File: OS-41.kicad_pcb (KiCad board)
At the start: 4 copper layers, 45.2 x 55.8 mm, 79 parts, among them J1 Conn_01x02_Pin, J2 Conn_01x02_Pin, J3 Conn_01x02_Pin, J4 Conn_Coaxial, J5 Conn_01x02_Pin, J6 USB_B_Micro, J7 Conn_01x09_Pin, SW1 TS-1187A-B-A-B, SW2 TS-1187A-B-A-B, U1 GPS1003, U10 W25Q128JVS, U2 SI4432-B1-FMR, U3 MCP1640x-xCHY, U4 ATGM336H-5N31, U5 DS18B20, U6 BMP390L, U7 RP2040, U8 ABM8-272-T3_C20625731, U9 AMS1117-3.3, X1 SMD-3225_4P 30.000MHZ 10PF

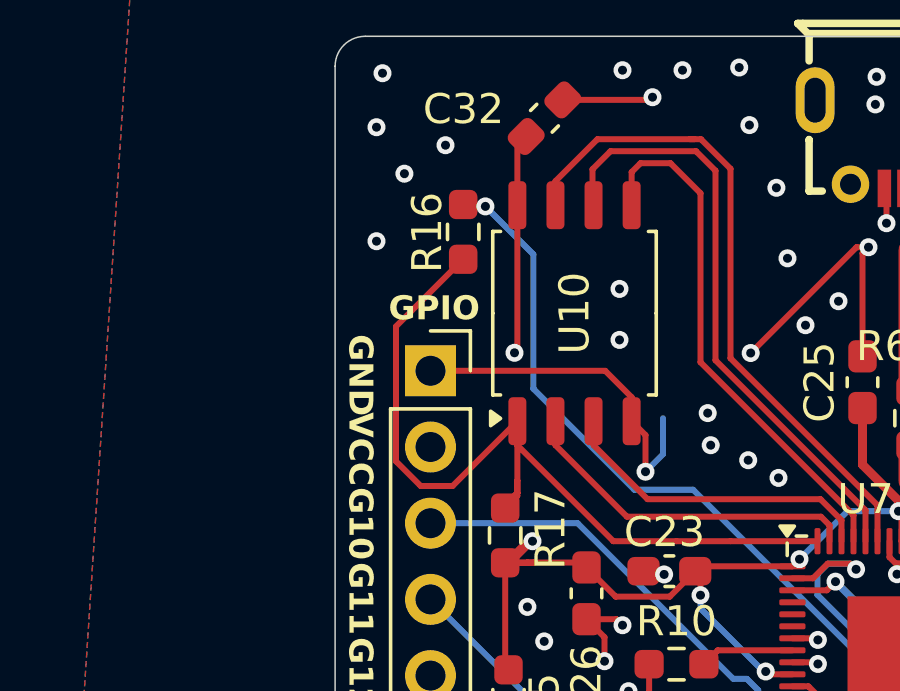
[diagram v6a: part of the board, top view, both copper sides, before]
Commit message: Fixed up some routing
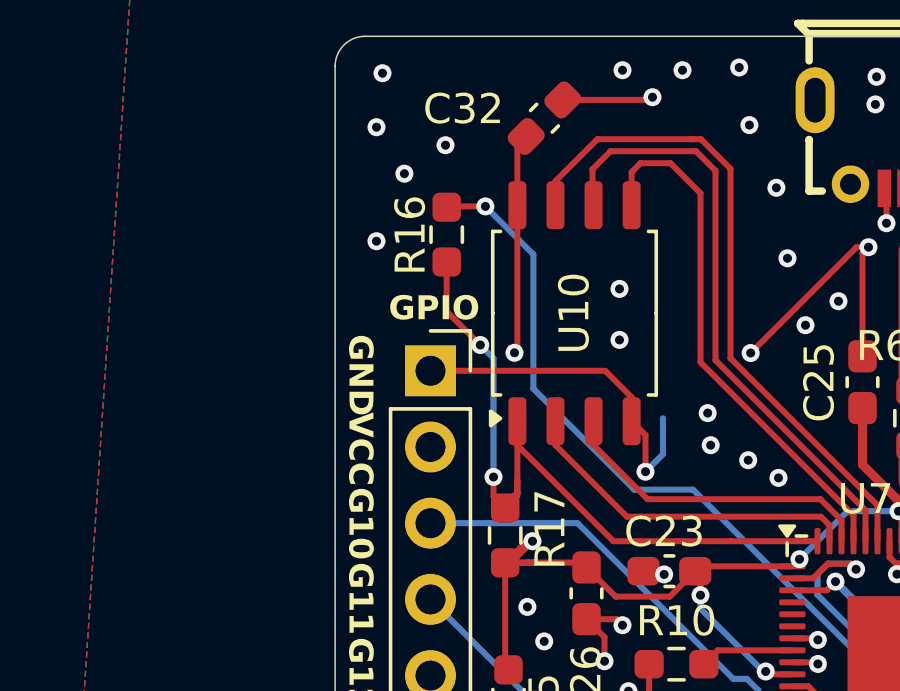
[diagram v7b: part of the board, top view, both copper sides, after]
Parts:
- moved R16 0.56 mm to (96.5, 93.0)
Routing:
- net QSPI_SS: track 29.9 -> 26.0 mm, vias 0 -> 2
- net USB_BOOT: track 44.3 -> 44.9 mm
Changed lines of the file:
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@@
 	(footprint "Resistor_SMD:R_0603_1608Metric_Pad0.98x0.95mm_HandSolder"
 		(layer "F.Cu")
-		(at 97.09 92.89 -90)
+		(at 96.54 92.98 -90)
 		(descr "Resistor SMD 0603 (1608 Metric), square (rectangular) end terminal, IPC_7351 nominal with elongated pad for handsoldering. (Body size source: IPC-SM-782 page 72, https://www.pcb-3d.com/wordpress/wp-content/uploads/ipc-sm-782a_amendment_1_and_2.pdf), generated with kicad-footprint-generator")
 		(tags "resistor handsolder")
@@
 	)
 	(segment
-		(start 97.1525 92.04)
-		(end 97.09 91.9775)
+		(start 97.83 92.04)
+		(end 96.5675 92.04)
 		(width 0.2)
 		(layer "F.Cu")
@@
 	)
 	(segment
-		(start 97.83 92.04)
-		(end 97.1525 92.04)
+		(start 121.55 109.8075)
+		(end 121.55 109.27)
 		(width 0.2)
 		(layer "F.Cu")
@@
 	)
 	(segment
-		(start 121.55 109.8075)
-		(end 121.55 109.27)
+		(start 96.5675 92.04)
+		(end 96.54 92.0675)
 		(width 0.2)
 		(layer "F.Cu")
@@
 	)
 	(segment
-		(start 96.735 101.36)
-		(end 98.895 99.2)
+		(start 98.895 99.2)
+		(end 98.895 99.999999)
 		(width 0.2)
 		(layer "F.Cu")
@@
 	)
 	(segment
-		(start 98.895 99.2)
-		(end 98.895 99.999999)
+		(start 96.54 93.8925)
+		(end 96.54 95.54)
 		(width 0.2)
 		(layer "F.Cu")
@@
 	)
 	(segment
-		(start 94.85 96.0425)
-		(end 94.85 100.536347)
-		(width 0.2)
-		(layer "F.Cu")
-		(net 33)
-	)
-	(segment
 		(start 98.895 101.69)
 		(end 98.49 102.095)
@@
 	)
 	(segment
-		(start 97.09 93.8025)
-		(end 94.85 96.0425)
+		(start 98.1 101.705)
+		(end 98.49 102.095)
 		(width 0.2)
 		(layer "F.Cu")
@@
 	)
 	(segment
-		(start 94.85 100.536347)
-		(end 95.673653 101.36)
+		(start 98.1 101.06)
+		(end 98.1 101.705)
 		(width 0.2)
 		(layer "F.Cu")
@@
 	)
 	(segment
-		(start 98.895 101.18)
-		(end 98.895 101.69)
+		(start 96.54 95.54)
+		(end 97.66 96.66)
 		(width 0.2)
 		(layer "F.Cu")
@@
 	)
 	(segment
-		(start 95.673653 101.36)
-		(end 96.735 101.36)
+		(start 98.895 101.18)
+		(end 98.895 101.69)
 		(width 0.2)
 		(layer "F.Cu")
@@
 		(net 33)
 	)
+	(via
+		(at 98.1 101.06)
+		(size 0.6)
+		(drill 0.3)
+		(layers "F.Cu" "B.Cu")
+		(net 33)
+	)
+	(via
+		(at 97.66 96.66)
+		(size 0.6)
+		(drill 0.3)
+		(layers "F.Cu" "B.Cu")
+		(net 33)
+	)
+	(segment
+		(start 97.66 96.66)
+		(end 98.1 97.1)
+		(width 0.2)
+		(layer "B.Cu")
+		(net 33)
+	)
+	(segment
+		(start 98.1 97.1)
+		(end 98.1 101.06)
+		(width 0.2)
+		(layer "B.Cu")
+		(net 33)
+	)

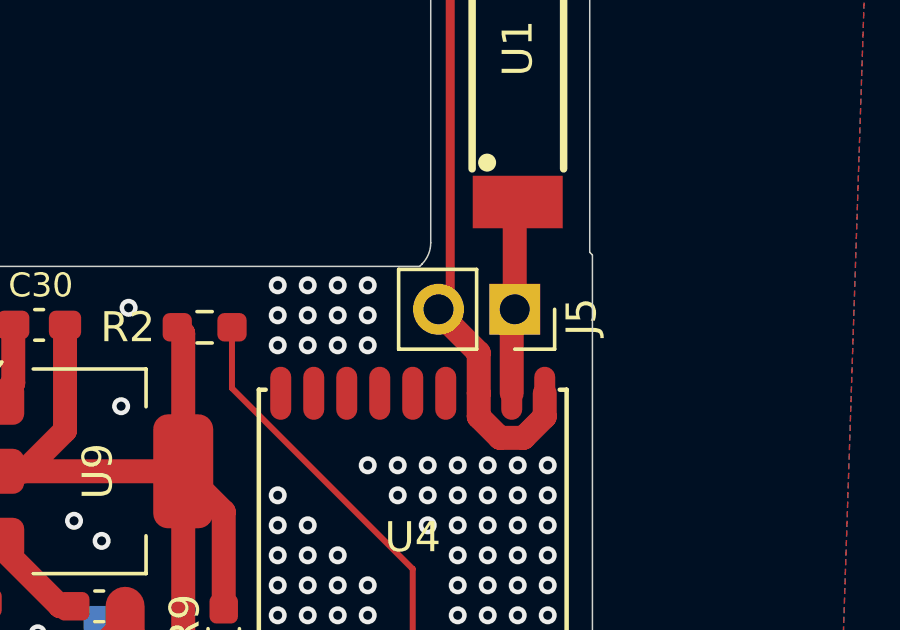
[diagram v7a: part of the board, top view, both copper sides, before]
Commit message: Add GPS ANT text
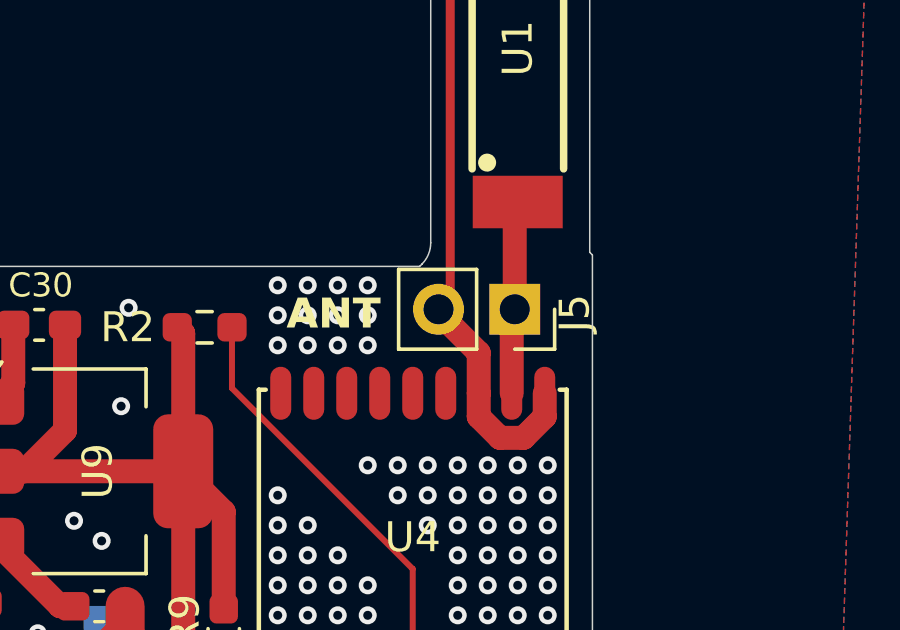
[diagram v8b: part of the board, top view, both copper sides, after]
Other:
- board text added: "ANT"
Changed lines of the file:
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@@
 		(tags "Through hole socket strip THT 1x02 2.54mm single row")
 		(property "Reference" "J5"
-			(at 0.25 -2.23 90)
+			(at 0.13 -2 90)
 			(layer "F.SilkS")
 			(effects
@@
 				(bold yes)
 			)
+			(justify left bottom)
+		)
+	)
+	(gr_text "ANT"
+		(at 127.79 88.53 0)
+		(layer "F.SilkS")
+		(effects
+			(font
+				(size 1 1)
+				(thickness 0.2)
+				(bold yes)
+			)
